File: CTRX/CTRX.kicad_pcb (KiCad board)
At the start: 2 copper layers, 45 x 19 mm, 32 parts, among them J2 SMA_CONNECTOR, J3 Conn_02x05_Odd_Even, U1 nRF52820-QDxx, U2 NRF21540-QDAA-R7, U3 USBLC6-2SC6, U4 ME6211C33M5, Y1 32MHz

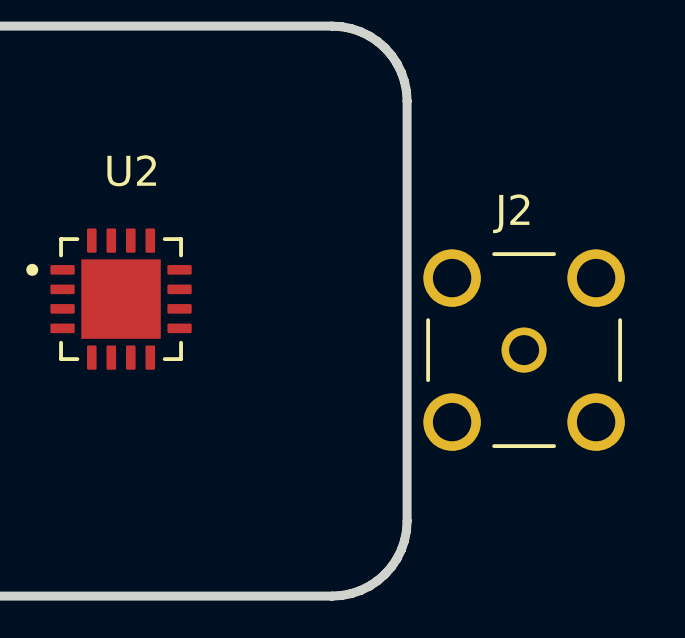
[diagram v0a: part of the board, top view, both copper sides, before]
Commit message: sma edge added
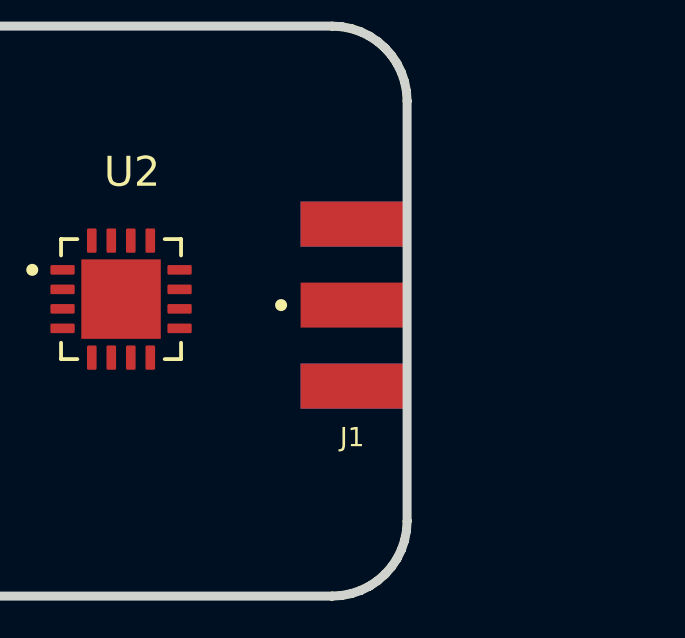
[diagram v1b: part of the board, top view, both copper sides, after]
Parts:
- removed J2: SMA_CONNECTOR, LPRS_SMA_CONNECTOR:LPRS_SMA_CONNECTOR
- added J1: CON-SMA-EDGE-S, SMA-EDGE:RFSOLUTIONS_CON-SMA-EDGE-S, F.Cu at (157.7, 88.1)

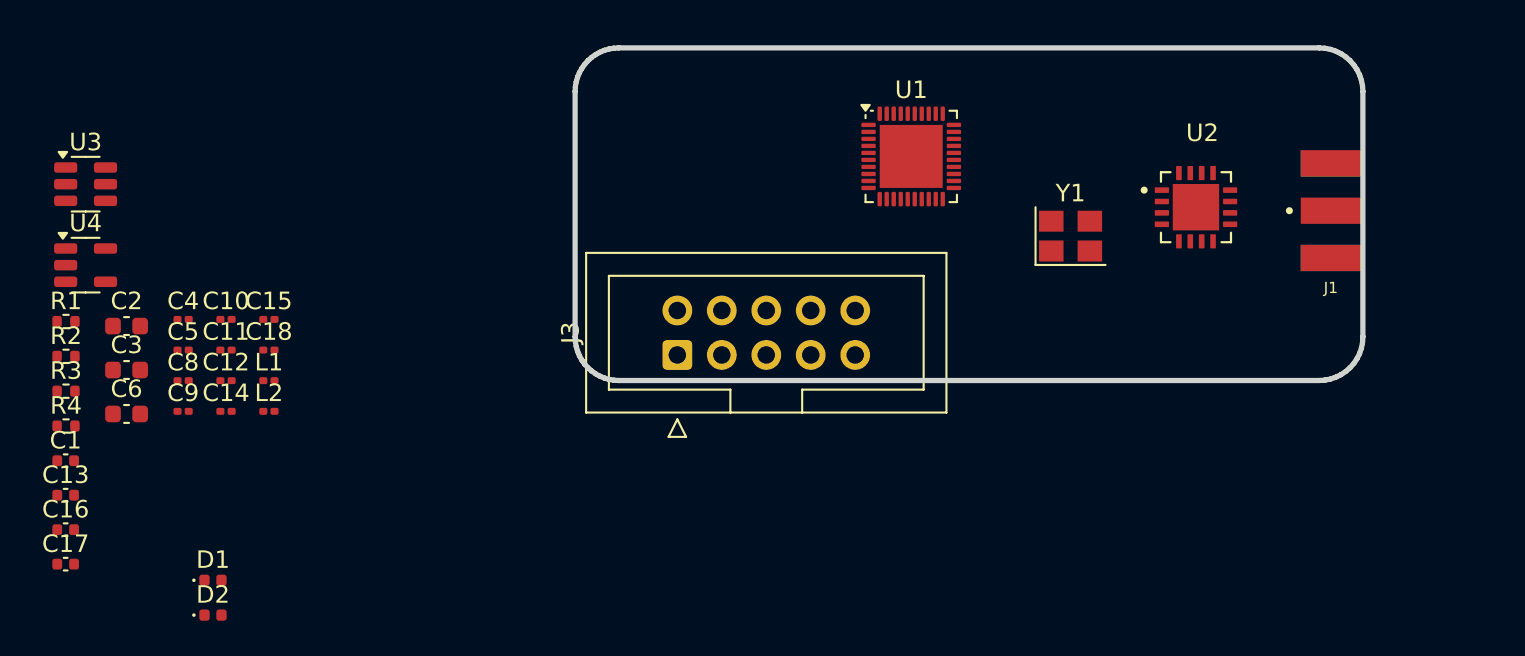
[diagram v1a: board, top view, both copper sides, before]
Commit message: capacitor covers were changed 0201->0402, pcb drawing was started
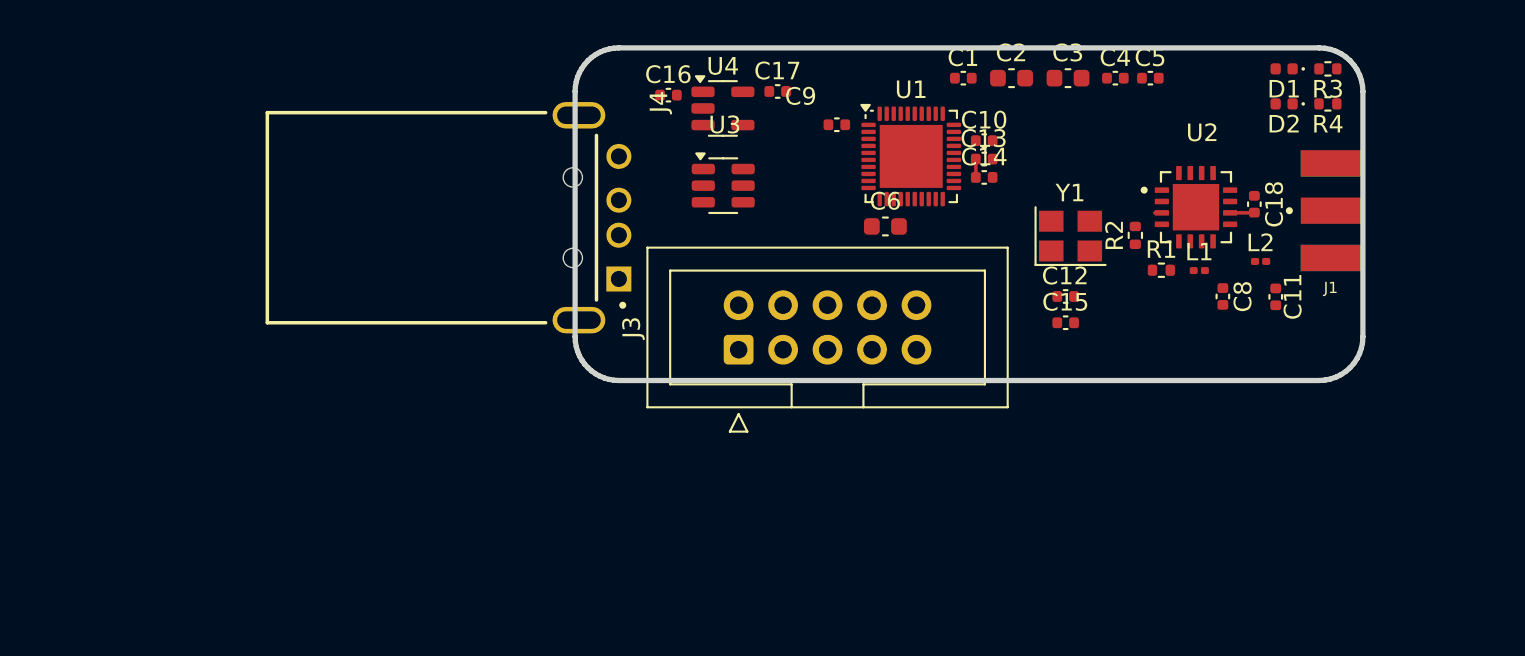
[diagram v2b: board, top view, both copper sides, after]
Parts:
- added J4: USB-AM-S-X-X-TH, USB-AM-S-X-X-TH:SAMTEC_USB-AM-S-X-X-TH, F.Cu at (114.7, 88.5)
- C10, C11, C12, C14, C15, C18, C4, C5, C8, C9: footprint Capacitor_SMD:C_0201_0603Metric -> Capacitor_SMD:C_0402_1005Metric
- moved R3 74.4 mm to (157.5, 80.0), turned to 180 degrees
- moved R4 74.4 mm to (157.5, 82.0), turned to 180 degrees
- moved D1 67.8 mm to (155.0, 80.0), turned to 180 degrees
- moved D2 67.8 mm to (155.0, 82.0), turned to 180 degrees
- moved R1 62.6 mm to (148.0, 91.5)
- moved R2 61.5 mm to (146.5, 89.5), turned to 90 degrees
- moved C11 60.0 mm to (154.5, 93.0), turned to -90 degrees
- moved C8 59.6 mm to (151.5, 93.0), turned to -90 degrees
- moved C5 57.4 mm to (147.4, 80.5)
- moved L2 57.3 mm to (153.7, 91.0)
- moved C18 56.9 mm to (153.3, 87.7), turned to -90 degrees
- moved C3 56.3 mm to (142.7, 80.5)
- moved C13 55.9 mm to (137.9, 85.2)
- moved C1 55.7 mm to (136.7, 80.5)
- moved C4 55.0 mm to (145.4, 80.5)
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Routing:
- net Net-(U2-TRX): track 0.00 -> 1.39 mm
- net DEC4: track 0.00 -> 1.05 mm
- net Net-(C11-Pad1): track 0.00 -> 1.00 mm
- net GND: track 0.00 -> 0.68 mm
- net +3.3V: track 0.00 -> 0.50 mm

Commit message: CTRX updated
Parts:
- removed C2: 4.7uF, Capacitor_SMD:C_0603_1608Metric
- D1, D2: footprint LED_SMD:LED_0402_1005Metric -> LED_SMD:LED_0805_2012Metric
- L1, L2: footprint Inductor_SMD:L_0201_0603Metric -> Inductor_SMD:L_0402_1005Metric
- moved R3 28.0 mm to (129.6, 83.1), turned to -90 degrees
- moved R4 27.9 mm to (129.6, 80.9), turned to 90 degrees
- moved D1 23.2 mm to (132.0, 83.1), turned to 0 degrees
- moved D2 23.0 mm to (132.0, 80.9), turned to 0 degrees
- moved C3 15.8 mm to (129.4, 89.1), turned to 90 degrees
- moved C4 15.6 mm to (131.0, 86.4), turned to -90 degrees
- moved C5 15.6 mm to (133.0, 86.4), turned to -90 degrees
- moved C15 13.2 mm to (142.7, 81.3), turned to 90 degrees
- moved C12 11.8 mm to (137.3, 82.4), turned to -90 degrees
- moved C18 9.33 mm to (144.0, 87.6), turned to 0 degrees
- moved C13 8.63 mm to (145.2, 80.6)
- moved C14 8.63 mm to (145.2, 81.6)
- moved Y1 8.37 mm to (140.0, 81.7)
- moved C1 7.55 mm to (132.0, 86.4), turned to 90 degrees
- moved C10 7.46 mm to (145.2, 82.7)
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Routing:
- net Net-(U2-TRX): track 1.39 -> 0.00 mm
- net DEC4: track 1.05 -> 0.00 mm
- net Net-(C11-Pad1): track 1.00 -> 0.00 mm
- added copper zone on F.Cu, net GND
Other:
- copper layers 2 -> 4

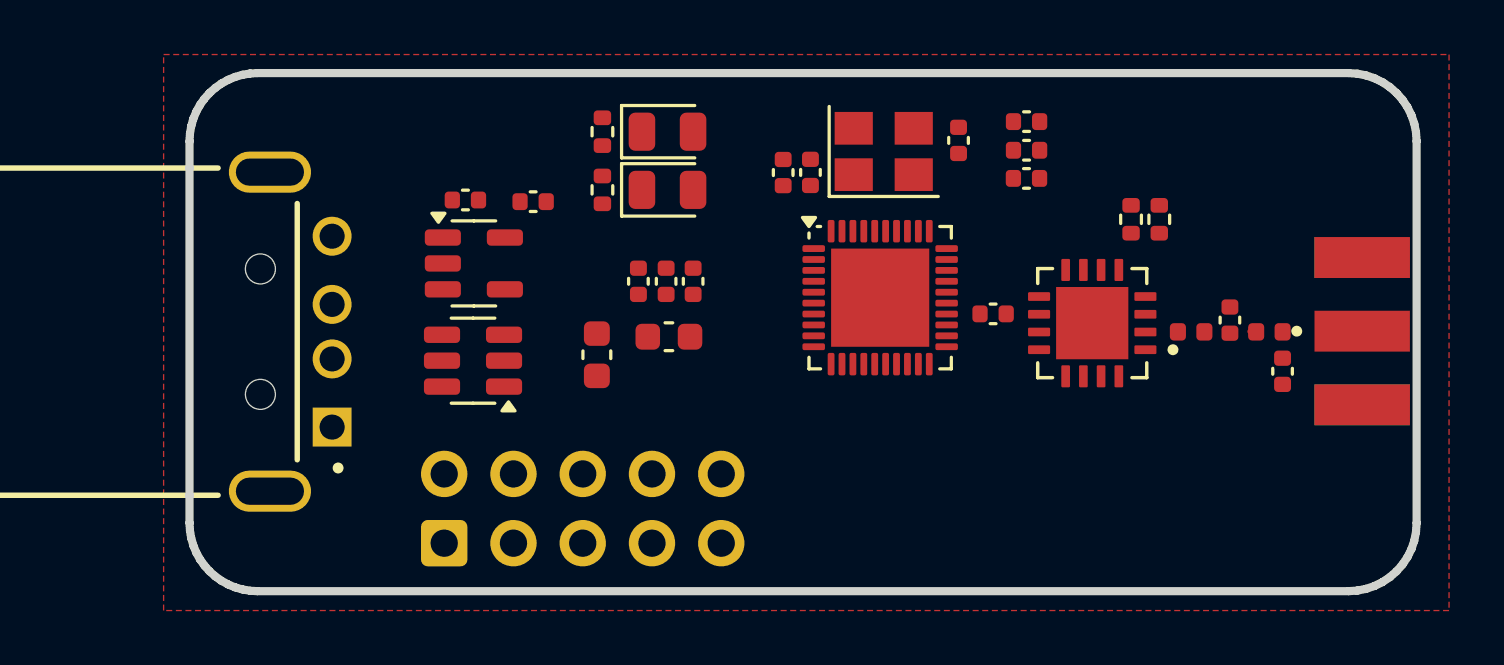
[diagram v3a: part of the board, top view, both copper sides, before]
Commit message: Placement refactor | Zones added
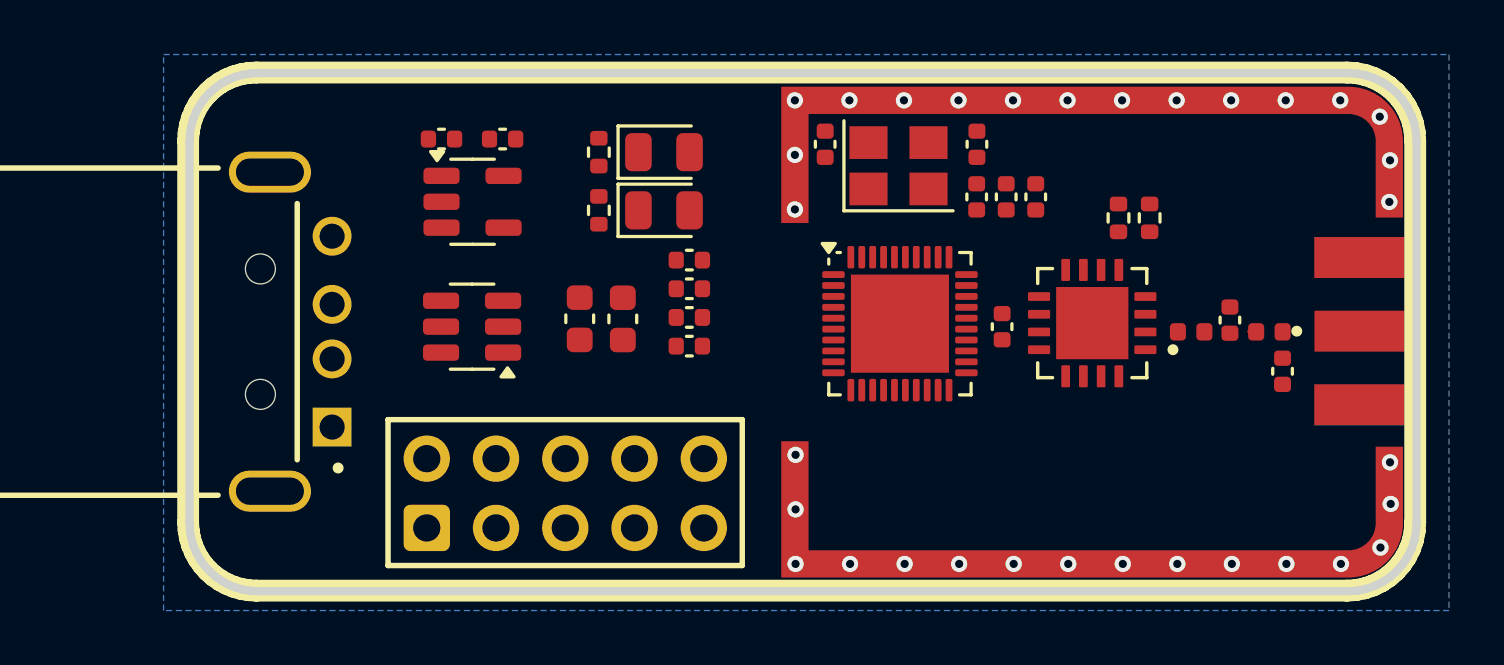
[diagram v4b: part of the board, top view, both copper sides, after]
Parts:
- moved C9 4.71 mm to (132.8, 85.7), turned to 180 degrees
- moved C6 3.34 mm to (128.8, 87.8), turned to 90 degrees
- moved C13 2.78 mm to (145.5, 83.3), turned to 90 degrees
- moved C17 2.55 mm to (126.0, 81.2), turned to 180 degrees
- moved C16 2.40 mm to (123.7, 81.2)
- moved C5 2.38 mm to (132.8, 88.8), turned to 180 degrees
- moved U4 2.26 mm to (124.9, 83.5)
- moved C10 1.95 mm to (143.4, 83.3), turned to 90 degrees
- moved C4 1.89 mm to (132.8, 86.7), turned to 180 degrees
- moved C14 1.87 mm to (144.4, 83.3), turned to 90 degrees
- moved C3 1.62 mm to (130.4, 87.8)
- moved C1 1.58 mm to (132.8, 87.8), turned to 0 degrees
- moved U3 1.25 mm to (124.9, 88.1)
- moved U1 1.20 mm to (140.6, 88.0)
- moved C12 1.16 mm to (137.8, 81.4)
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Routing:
- net GND: vias 0 -> 32
- added copper zone on In2.Cu, net +3.3V
- added copper zone on B.Cu, net GND
- added copper zone on In1.Cu, net GND
- removed copper zone on F.Cu, net GND
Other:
- board text added: "CTRX"
- board text added: "YENIAY"

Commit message: antenna
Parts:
- C11, C18, C8: footprint Capacitor_SMD:C_0402_1005Metric -> Capacitor_SMD:C_0201_0603Metric
- C12, C15: value 12pF -> 8pF
- L1, L2: footprint Inductor_SMD:L_0402_1005Metric -> Inductor_SMD:L_0201_0603Metric
- moved C11 1.10 mm to (154.6, 88.6)
- moved L2 0.70 mm to (153.4, 88.3)
- moved C8 0.46 mm to (152.2, 87.9)
- moved L1 0.23 mm to (151.0, 88.3)

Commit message: ready
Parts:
- added C2: 1pF, Capacitor_SMD:C_0201_0603Metric, F.Cu at (142.5, 90.0)
- added C7: 1.2pF, Capacitor_SMD:C_0201_0603Metric, F.Cu at (143.9, 90.0)
- added L3: 4.7nH, Inductor_SMD:L_0201_0603Metric, F.Cu at (142.8, 88.9)
- added L4: 2.2nH, Inductor_SMD:L_0201_0603Metric, F.Cu at (144.3, 88.9)
- moved C6 12.2 mm to (138.6, 95.0), turned to 0 degrees
- moved C15 5.54 mm to (137.8, 81.4), turned to -90 degrees
- moved C12 5.42 mm to (143.2, 81.4), turned to 90 degrees
- moved C17 3.49 mm to (122.6, 82.1), turned to -90 degrees
- moved C16 3.29 mm to (122.6, 84.3), turned to -90 degrees
- moved R2 2.72 mm to (152.3, 84.9)
- moved L1 2.09 mm to (152.7, 89.5)
- moved R1 2.09 mm to (147.5, 85.9), turned to 0 degrees
- moved U2 2.04 mm to (149.2, 89.2)
- moved C11 2.03 mm to (154.5, 90.7)
- moved U1 1.73 mm to (138.9, 88.3)
- moved C18 1.64 mm to (145.7, 88.9), turned to 0 degrees
- moved L2 1.47 mm to (154.2, 89.5)
- moved J1 1.32 mm to (157.7, 89.6)
- moved C8 1.31 mm to (153.4, 88.4)
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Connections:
- U1 pad 24: NRF_ANT -> Net-(U1-ANT)
- U1 pad 9: +3.3V -> +5V
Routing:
- net +3.3V: track 0.50 -> 42.6 mm, vias 0 -> 8
- net +5V: track 0.00 -> 30.0 mm, vias 0 -> 1
- net NRF_PA_PDN: track 0.00 -> 18.8 mm, vias 0 -> 2
- net P014: track 0.00 -> 18.4 mm, vias 0 -> 1
- net NRF_SPI0_MISO: track 0.00 -> 18.4 mm, vias 0 -> 2
- net NRF_SWCLK: track 0.00 -> 18.2 mm, vias 0 -> 2
- net NRF_SPI0_CS: track 0.00 -> 17.3 mm, vias 0 -> 2
- net USB_D+: track 0.00 -> 17.2 mm
- net NRF_SPI0_SCK: track 0.00 -> 16.9 mm, vias 0 -> 2
- net NRF_SPI0_MOSI: track 0.00 -> 16.7 mm, vias 0 -> 2
- net P015: track 0.00 -> 14.2 mm, vias 0 -> 2
- net USB_D-: track 0.00 -> 14.0 mm
- net NRF_SWDIO: track 0.00 -> 12.6 mm, vias 0 -> 2
- net NRF_PA_RX_EN: track 0.00 -> 12.0 mm, vias 0 -> 2
- net NRF_LED1: track 0.00 -> 10.2 mm, vias 0 -> 2
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
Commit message: CTRX Order Ready
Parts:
- added C19: 4.7uF, Capacitor_SMD:C_0603_1608Metric, F.Cu at (129.2, 86.8)
- moved C4 12.3 mm to (144.9, 84.1), turned to 90 degrees
- moved C13 8.17 mm to (137.8, 83.4)
- moved C14 1.08 mm to (146.0, 84.1)
- moved C1 1.07 mm to (132.8, 86.7)
- moved C5 1.07 mm to (132.8, 87.7)
- moved J1 0.50 mm to (157.2, 89.5)
- turned U3 to 0 degrees
- turned U4 to 0 degrees
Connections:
- C1 pad 2: +5V -> +3.3V
- C3 pad 1: +5V -> +3.3V
- C4 pad 1: +5V -> +3.3V
- C5 pad 1: +5V -> +3.3V
- J3 pad 2: P014 -> NRF_SWDIO
- J3 pad 3: GND -> P014
- J3 pad 5: GND -> P015
- J3 pad 6: P015 -> unconnected-(J3-Pin_6-Pad6)
- J3 pad 8: NRF_SWDIO -> unconnected-(J3-Pin_8-Pad8)
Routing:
- net DEC4: track 6.63 -> 15.3 mm, vias 0 -> 3
- net NRF_SWDIO: track 12.6 -> 20.5 mm
- net USB_CONN_D-: track 0.00 -> 7.27 mm
- net USB_CONN_D+: track 0.52 -> 5.34 mm
- net NRF_PA_PDN: track 18.8 -> 15.3 mm
- net +3.3V: track 42.6 -> 45.5 mm, vias 8 -> 11
- net +5V: track 30.0 -> 32.8 mm, vias 1 -> 0
- net P014: track 18.4 -> 15.7 mm
- net NRF_SPI0_CS: track 17.3 -> 18.4 mm
- net NRF_XC2: track 8.09 -> 8.75 mm
- net NRF_XC1: track 9.94 -> 10.5 mm
- net P015: track 14.2 -> 13.7 mm, vias 2 -> 1
- net Net-(U2-MODE): track 5.42 -> 5.46 mm, vias 3 -> 2
- net GND: track 0.25 -> 0.22 mm, vias 62 -> 68
- added copper zone on F.Cu, net GND

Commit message: ready to order.
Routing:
- net GND: track 0.22 -> 5.43 mm, vias 68 -> 66
- net NRF_NRST: track 7.62 -> 8.76 mm
- net NRF_SPI0_SCK: track 16.9 -> 17.9 mm
- net P015: track 13.7 -> 14.7 mm
- net NRF_SPI0_MOSI: track 16.7 -> 17.4 mm
- net NRF_PA_TX_EN: track 9.47 -> 10.2 mm
- net P014: track 15.7 -> 16.3 mm
- net NRF_PA_MODE: track 8.51 -> 7.93 mm
